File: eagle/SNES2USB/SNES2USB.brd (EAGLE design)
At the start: 50 x 50 mm, 42 parts, among them Y1 12-20MHz

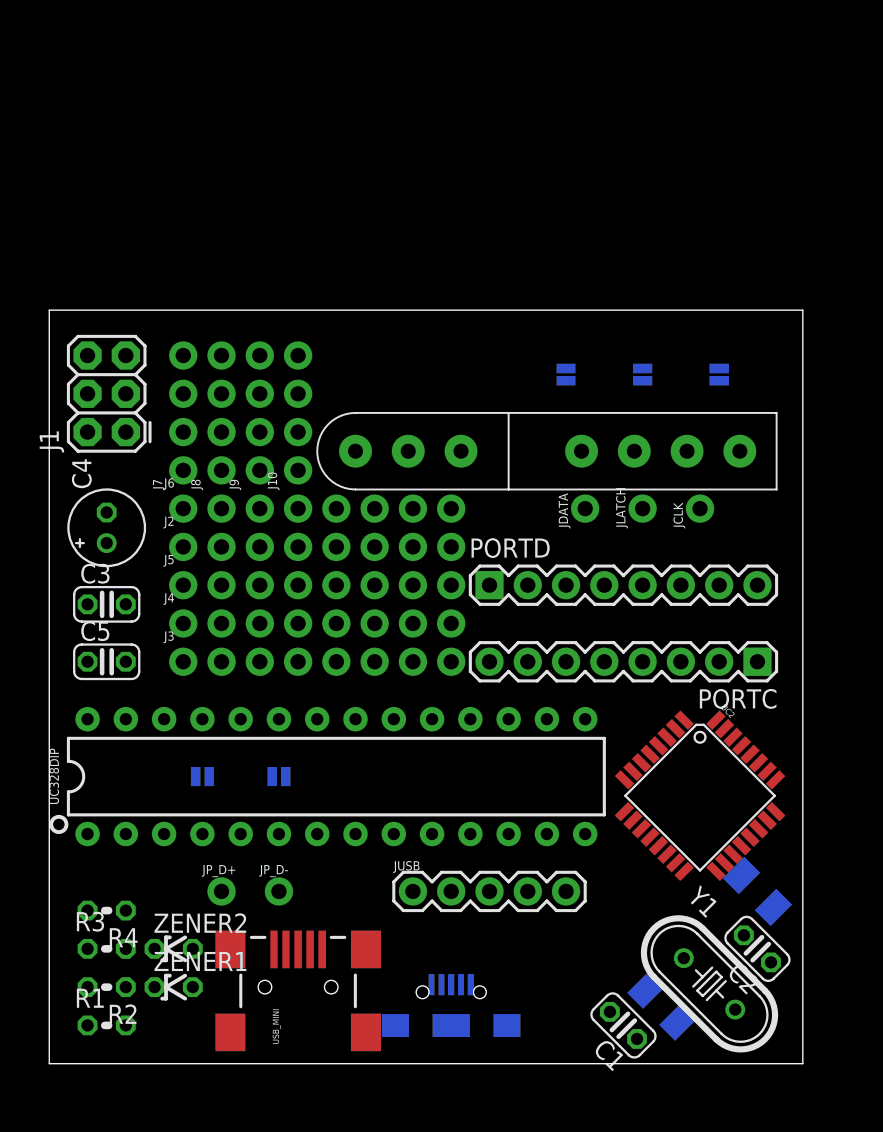
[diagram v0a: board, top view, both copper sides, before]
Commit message: SNES2USB nearly ready to be released, todo change for alternate layout of SNES pad
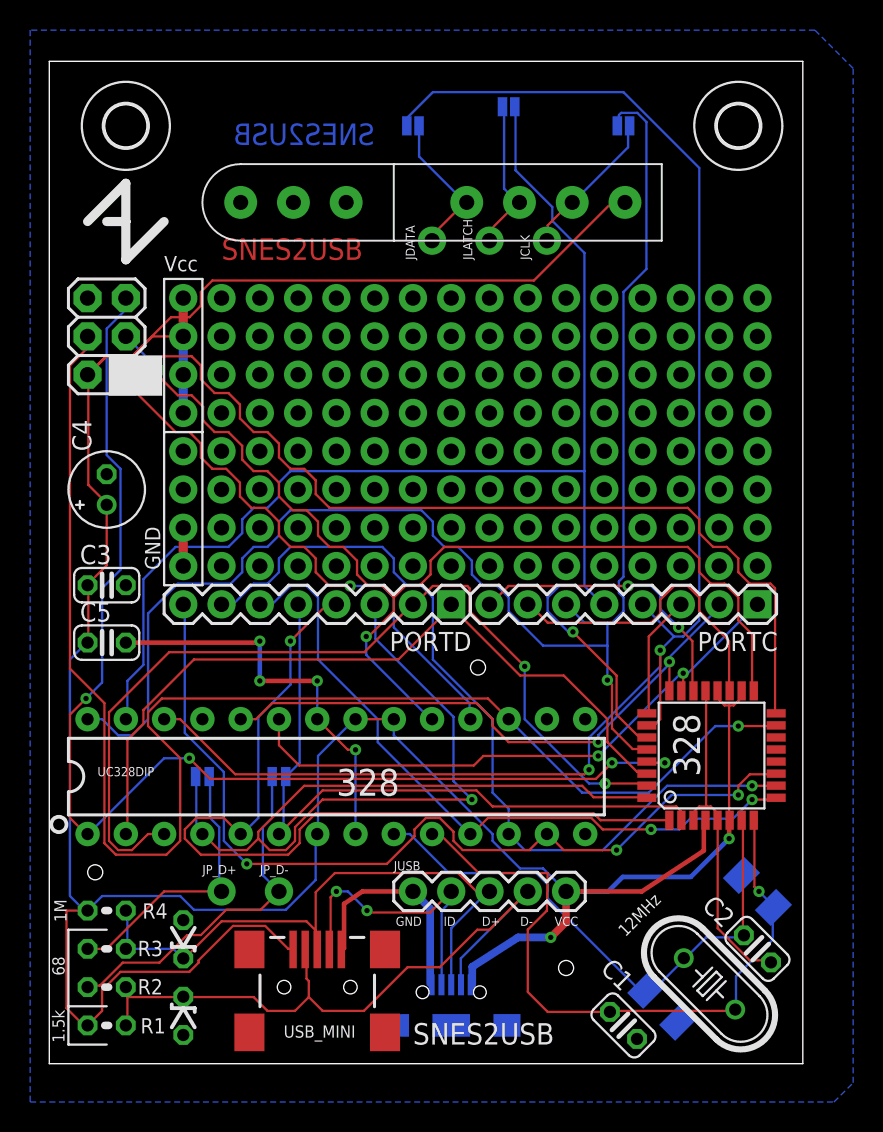
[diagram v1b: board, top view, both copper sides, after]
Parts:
- removed J6: (no value), SparkFun-Connectors:1X08_NO_SILK
- added H1, H4: MOUNT-HOLE2.8, holes:2,8
- added U$2: (no value), kalshagar-images:VUSB_LOGO
- J10, J7, J8, J9: device SparkFun-Connectors:1X04_NO_SILK -> SparkFun-Connectors:1X16_NO_SILK
- J2, J3, J4, J5: device SparkFun-Connectors:1X08_NO_SILK -> SparkFun-Connectors:1X16_NO_SILK
- moved JCLK 20.5 mm to (33.0, 54.6)
- moved JDATA 20.5 mm to (25.4, 54.6)
- moved JLATCH 20.5 mm to (29.2, 54.6)
- moved JPL 19.9 mm to (30.5, 63.5), turned to 180 degrees
- moved JPD 19.4 mm to (24.1, 62.2), turned to 0 degrees
- moved U$1 18.2 mm to (12.7, 57.1)
- moved JPC 17.7 mm to (38.1, 62.2), turned to 0 degrees
- moved J10 13.7 mm to (8.89, 50.8), turned to 0 degrees
- moved J9 10.2 mm to (8.89, 48.3), turned to 0 degrees
- moved J8 6.84 mm to (8.89, 45.7), turned to 0 degrees
- moved J2 6.35 mm to (8.89, 40.6)
- moved J3 6.35 mm to (8.89, 33.0)
- moved J4 6.35 mm to (8.89, 35.6)
- moved J5 6.35 mm to (8.89, 38.1)
- moved J1 3.81 mm to (5.08, 45.7)
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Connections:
- net GND: now also J2.1, J3.1, J4.1, J5.1
- net VCC: now also J10.1, J7.1, J8.1, J9.1
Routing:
- net VCC: track 0.00 -> 216.2 mm, vias 0 -> 2
- net C3: track 0.00 -> 104.5 mm, vias 0 -> 2
- net C5: track 0.00 -> 102.5 mm, vias 0 -> 1
- net MISO: track 0.00 -> 98.0 mm, vias 0 -> 1
- net MOSI: track 0.00 -> 96.7 mm, vias 0 -> 1
- net C4: track 0.00 -> 94.0 mm, vias 0 -> 1
- net RESET: track 0.00 -> 81.0 mm, vias 0 -> 4
- net SCK: track 0.00 -> 72.0 mm, vias 0 -> 2
- net D2: track 0.00 -> 68.4 mm, vias 0 -> 1
- net GND: track 0.00 -> 66.4 mm, vias 0 -> 4
- net D1: track 0.00 -> 60.5 mm, vias 0 -> 2
- net D7: track 0.00 -> 60.3 mm, vias 0 -> 3
- net D3: track 0.00 -> 57.8 mm, vias 0 -> 1
- net D6: track 0.00 -> 55.8 mm, vias 0 -> 1
- net D0: track 0.00 -> 50.7 mm
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- added copper zone on layer 16, net GND
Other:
- board size 50 x 50 mm -> 50 x 66.5 mm
- board text added: "1.5k"
- board text added: "12MHz"
- board text added: "1M"
- board text added: "328"
- board text added: "68"
- board text added: "D+"
- board text added: "D-"
- board text added: "GND"
- board text added: "ID"
- board text added: "SNES2USB"
- board text added: "USB_Micro"
- board text added: "VCC"
- board text added: "Vcc"
- board text added: "http://electrogeek.cc/snes%20pad%20usb%20adapter.html"
- board text added: "v1.0 - Feb2020"
